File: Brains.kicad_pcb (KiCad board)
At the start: 4 copper layers, 81.5 x 50.5 mm, 49 parts, among them J1 Conn_01x02_Pin, J3 USB_B_Micro, SW1 SW_SPST, SW2 SW_SPST, U1 ESP32-S3-WROOM-1, U2 LM78M05_TO220, U3 AMS1117-3.3, U5 USBLC6-2SC6, U6 W25Q16JVSS

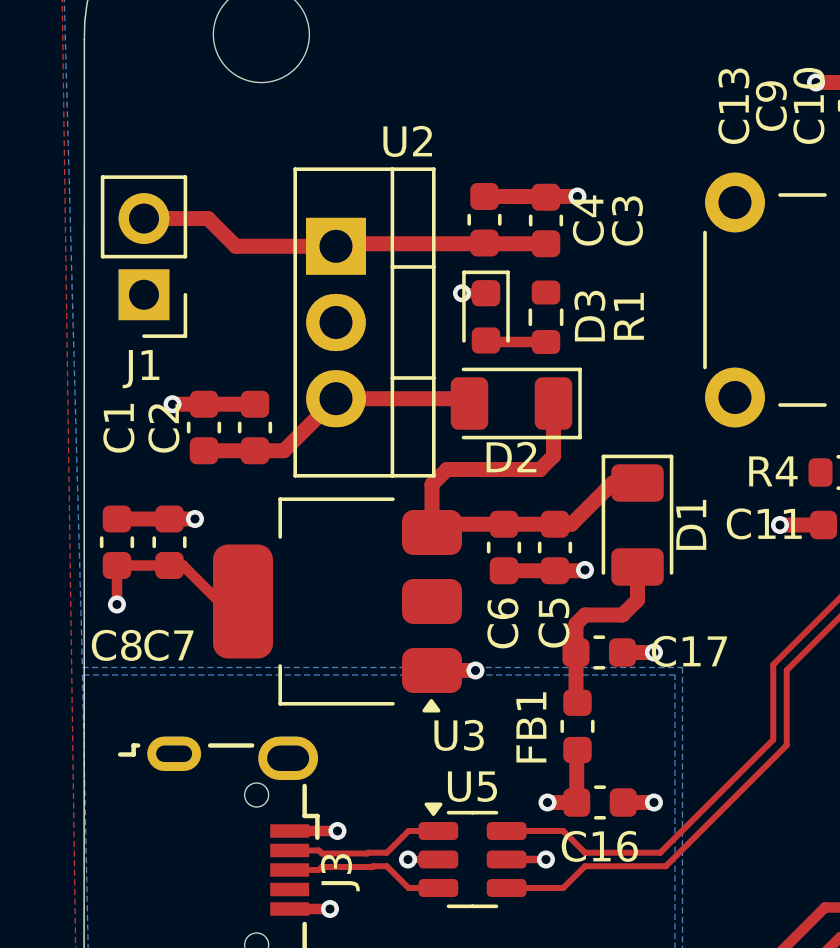
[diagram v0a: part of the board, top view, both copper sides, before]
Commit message: Changed LDO to AP2112K-3.3, Updated Layout
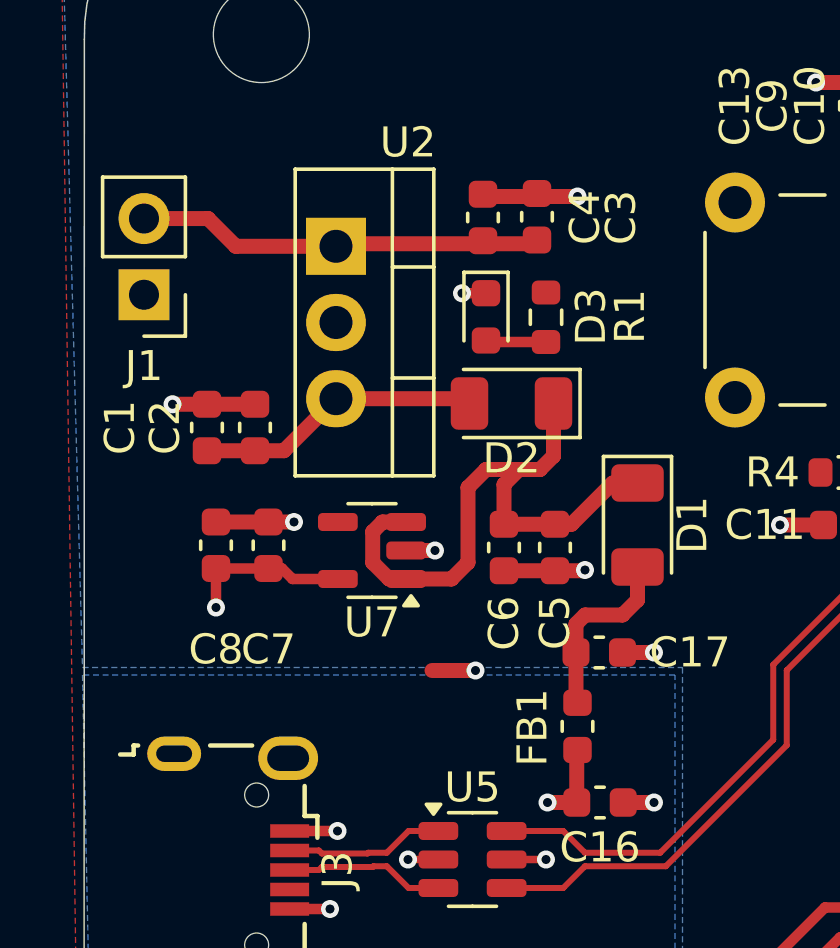
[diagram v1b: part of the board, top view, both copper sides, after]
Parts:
- removed U3: AMS1117-3.3, Package_TO_SOT_SMD:SOT-223-3_TabPin2
- added U7: AP2112K-3.3, Package_TO_SOT_SMD:SOT-23-5, F.Cu at (104.4, 75.6)
- C1, C3, C5, C8: value tbd -> 10uF
- C2, C4, C6, C7: value tbd -> 1uF
- moved C7 3.30 mm to (101.0, 75.4)
- moved C8 3.30 mm to (99.2, 75.4)
- moved C3 0.32 mm to (109.9, 64.5)
- moved C1 0.10 mm to (98.9, 71.5)
- moved C4 0.09 mm to (108.1, 64.5)
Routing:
- net 5Vin: track 15.3 -> 20.5 mm
- net GND: track 39.9 -> 40.9 mm, vias 27 -> 28
